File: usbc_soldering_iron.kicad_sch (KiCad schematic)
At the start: 87 parts, among them J1 DBG, J2 TIP_L, J3 USB_C_Receptacle_USB2.0_14P, J4 TIP_H, J5 TIP_K, J6 OLED, J7 LED RING, Q1 DMP6023LE, Q2 MMBT3904, SW1 RST, SW2 B1, SW3 B2, SW4 B3, SW5 BS, U1 SRV05-4, U2 MCP6001-OT, U3 CH32V203GxUx, U4 AP63201WU, U5 FUSB302BMPX, U6 TLV333IDBVR, U7 SC7A20

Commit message: board dimensions and different components
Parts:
- removed C1, C12, C15: 100n, Capacitor_SMD:C_0805_2012Metric, symbol Device:C_Small
- removed C5: 22u, Capacitor_SMD:C_0805_2012Metric, symbol Device:C_Small
- removed Q1: DMP6023LE, Package_TO_SOT_SMD:SOT-223-3_TabPin2, symbol Transistor_FET:Q_PMOS_GDS
- removed SW1: RST, Button_Switch_SMD:SW_SPST_TS-1088-xR020, symbol Switch:SW_Push
- removed SW4: B3, Button_Switch_SMD:SW_SPST_TS-1088-xR020, symbol Switch:SW_Push
- removed U1: SRV05-4, Package_TO_SOT_SMD:SOT-23-6, symbol Power_Protection:SRV05-4
- added H1, H2: MountingHole, MountingHole:MountingHole_2.2mm_M2, symbol Mechanical:MountingHole
- added Q3: DMP3013SFV, Package_SON:Diodes_PowerDI3333-8, symbol Transistor_FET:DMP3013SFV
- added TP1, TP7: TP_PD1, TestPoint:TestPoint_Pad_D1.0mm, symbol Connector:TestPoint
- added U8: TPD4E05U06DQA, Package_SON:USON-10_2.5x1.0mm_P0.5mm, symbol Power_Protection:TPD4E05U06DQA
- C1: renamed from C8; footprint Capacitor_SMD:C_0805_2012Metric -> Capacitor_SMD:C_0603_1608Metric
- C10: renamed from C3; footprint Capacitor_SMD:C_0805_2012Metric -> Capacitor_SMD:C_0603_1608Metric
- C11: renamed from C14; footprint Capacitor_SMD:C_0805_2012Metric -> Capacitor_SMD:C_0603_1608Metric
- C12: renamed from C6; footprint Capacitor_SMD:C_0805_2012Metric -> Capacitor_SMD:C_0603_1608Metric
- C13: renamed from C32; footprint Capacitor_SMD:C_0805_2012Metric -> Capacitor_SMD:C_0603_1608Metric
- C15: renamed from C34; footprint Capacitor_SMD:C_0805_2012Metric -> Capacitor_SMD:C_0603_1608Metric
- C16: renamed from C33; footprint Capacitor_SMD:C_0805_2012Metric -> Capacitor_SMD:C_0603_1608Metric
- C17: renamed from C29; footprint Capacitor_SMD:C_0805_2012Metric -> Capacitor_SMD:C_0603_1608Metric
- C18: renamed from C26; footprint Capacitor_SMD:C_0805_2012Metric -> Capacitor_SMD:C_0603_1608Metric
- C19: renamed from C27; footprint Capacitor_SMD:C_0805_2012Metric -> Capacitor_SMD:C_0603_1608Metric
- C2: renamed from C9; footprint Capacitor_SMD:C_0805_2012Metric -> Capacitor_SMD:C_0603_1608Metric
- C20: renamed from C28; footprint Capacitor_SMD:C_0805_2012Metric -> Capacitor_SMD:C_0603_1608Metric
- C21: renamed from C30; footprint Capacitor_SMD:C_0805_2012Metric -> Capacitor_SMD:C_0603_1608Metric
- C22: renamed from C31; footprint Capacitor_SMD:C_0805_2012Metric -> Capacitor_SMD:C_0603_1608Metric
- C23: footprint Capacitor_SMD:C_0805_2012Metric -> Capacitor_SMD:C_0603_1608Metric
- C28: renamed from C24; footprint Capacitor_SMD:C_0805_2012Metric -> Capacitor_SMD:C_0603_1608Metric
- C3: renamed from C7; footprint Capacitor_SMD:C_0805_2012Metric -> Capacitor_SMD:C_0603_1608Metric
- C30: renamed from C16; footprint Capacitor_SMD:C_0805_2012Metric -> Capacitor_SMD:C_0603_1608Metric
- C31: renamed from C25; footprint Capacitor_SMD:C_0805_2012Metric -> Capacitor_SMD:C_0603_1608Metric
- C32: renamed from C21; footprint Capacitor_SMD:C_0805_2012Metric -> Capacitor_SMD:C_0603_1608Metric
- C5: renamed from C11; footprint Capacitor_SMD:C_0805_2012Metric -> Capacitor_SMD:C_0603_1608Metric
- C6: renamed from C10; footprint Capacitor_SMD:C_0805_2012Metric -> Capacitor_SMD:C_0603_1608Metric
- C7: renamed from C2; footprint Capacitor_SMD:C_0805_2012Metric -> Capacitor_SMD:C_0603_1608Metric
- C9: renamed from C13; footprint Capacitor_SMD:C_0805_2012Metric -> Capacitor_SMD:C_0603_1608Metric
- J1: renamed from J3; footprint Connector_USB:USB_C_Receptacle_G-Switch_GT-USB-7010ASV -> Connector_USB:USB_C_Receptacle_G-Switch_GT-USB-7025
- L1: footprint Inductor_SMD:L_0805_2012Metric -> Inductor_SMD:L_Changjiang_FTC201607S
- R1: footprint Resistor_SMD:R_0805_2012Metric -> Resistor_SMD:R_0603_1608Metric
- R10: renamed from R22; footprint Resistor_SMD:R_0805_2012Metric -> Resistor_SMD:R_0603_1608Metric
- R11: renamed from R3; footprint Resistor_SMD:R_0805_2012Metric -> Resistor_SMD:R_0603_1608Metric
- R12: renamed from R4; footprint Resistor_SMD:R_0805_2012Metric -> Resistor_SMD:R_0603_1608Metric
- R13: renamed from R23; footprint Resistor_SMD:R_0805_2012Metric -> Resistor_SMD:R_0603_1608Metric
- R14: renamed from R21; footprint Resistor_SMD:R_0805_2012Metric -> Resistor_SMD:R_0603_1608Metric
- R15: renamed from R13; footprint Resistor_SMD:R_0805_2012Metric -> Resistor_SMD:R_0603_1608Metric
- R16: renamed from R14; footprint Resistor_SMD:R_0805_2012Metric -> Resistor_SMD:R_0603_1608Metric
- R17: renamed from R15; footprint Resistor_SMD:R_0805_2012Metric -> Resistor_SMD:R_0603_1608Metric
- R18: renamed from R16; footprint Resistor_SMD:R_0805_2012Metric -> Resistor_SMD:R_0603_1608Metric
- R19: renamed from R12; footprint Resistor_SMD:R_0805_2012Metric -> Resistor_SMD:R_0603_1608Metric
- R2: renamed from R5; footprint Resistor_SMD:R_0805_2012Metric -> Resistor_SMD:R_0603_1608Metric
- R20: renamed from R11; footprint Resistor_SMD:R_0805_2012Metric -> Resistor_SMD:R_0603_1608Metric
- R21: renamed from R10; footprint Resistor_SMD:R_0805_2012Metric -> Resistor_SMD:R_0603_1608Metric
- R22: renamed from R19; footprint Resistor_SMD:R_0805_2012Metric -> Resistor_SMD:R_0603_1608Metric
- R23: renamed from R20; footprint Resistor_SMD:R_0805_2012Metric -> Resistor_SMD:R_0603_1608Metric
- R25: renamed from R17; footprint Resistor_SMD:R_0805_2012Metric -> Resistor_SMD:R_0603_1608Metric
- R3: renamed from R6; footprint Resistor_SMD:R_0805_2012Metric -> Resistor_SMD:R_0603_1608Metric
- R4: renamed from R8; footprint Resistor_SMD:R_0805_2012Metric -> Resistor_SMD:R_0603_1608Metric
- R5: renamed from R7; footprint Resistor_SMD:R_0805_2012Metric -> Resistor_SMD:R_0603_1608Metric
- R6: renamed from R2; footprint Resistor_SMD:R_0805_2012Metric -> Resistor_SMD:R_0603_1608Metric
- R7: renamed from R24; footprint Resistor_SMD:R_0805_2012Metric -> Resistor_SMD:R_0603_1608Metric
- R8: renamed from R25; footprint Resistor_SMD:R_0805_2012Metric -> Resistor_SMD:R_0603_1608Metric
- R9: renamed from R18; footprint Resistor_SMD:R_0805_2012Metric -> Resistor_SMD:R_0603_1608Metric
- renumbered C4 to C14, C22 to C24, C20 to C25, C19 to C26, C18 to C27, C17 to C29, J1 to J2, J7 to J3, J6 to J4, J4 to J5, J5 to J6, J2 to J7, Q2 to Q1, R9 to R24, SW5 to SW4, TP1 to TP2, TP2 to TP3, TP3 to TP4, TP4 to TP5, TP5 to TP6, U3 to U1, U5 to U2, U7 to U5, U2 to U6, U6 to U7
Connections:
- net CC1: now also U8.5 (D2-)
- net CC2: now also U8.1 (D1+)
- net GND: now also U8.3 (GND), U8.8 (GND)
- net NRST: now also TP7.1
- net SHUNT_L: now also Q3.5 (D)
- net TIP_H: now also Q3.1 (S), Q3.2 (S), Q3.3 (S)
- net JDP: now reaches J1.A6 (D+), J1.B6 (D+), R3.1
- net JDP: now also U8.2 (D1-)
- net JDN: now reaches J1.A7 (D-), J1.B7 (D-), R2.1
- net JDN: now also U8.4 (D2+)
- net at R20.2, R21.1: now also Q3.4 (G)
- net BTN3 renamed PB3
- net PB3: now also TP1.1
- no-connect marks 2 -> 6
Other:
- note removed: "REVIEW"
- moved on the sheet: C11, C13, C3, R13, R2, R3, SW3, SW4

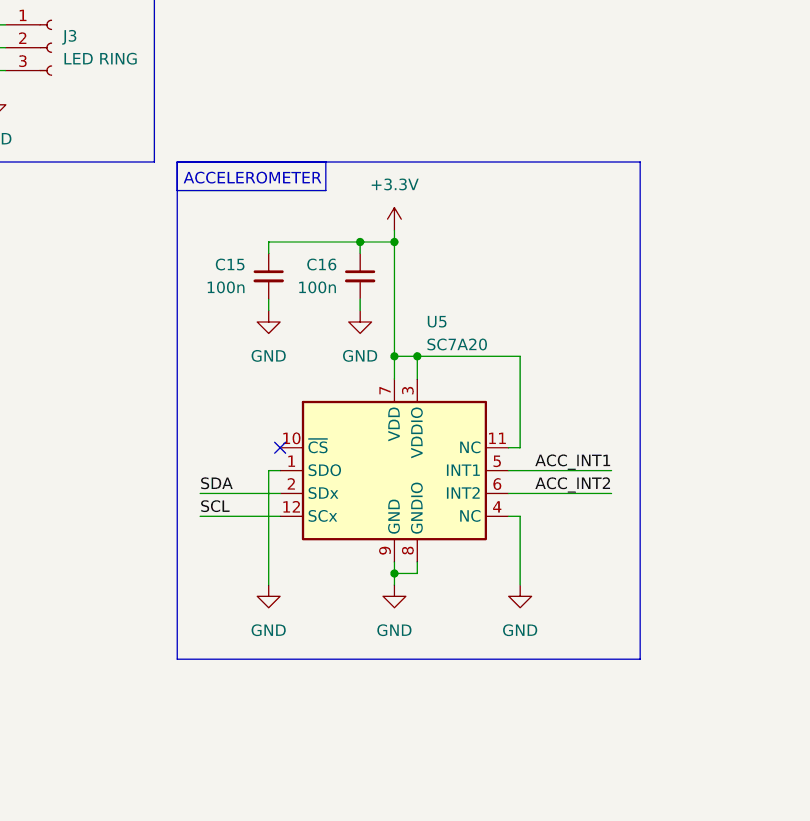
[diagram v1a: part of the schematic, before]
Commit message: some things needed to be 0805
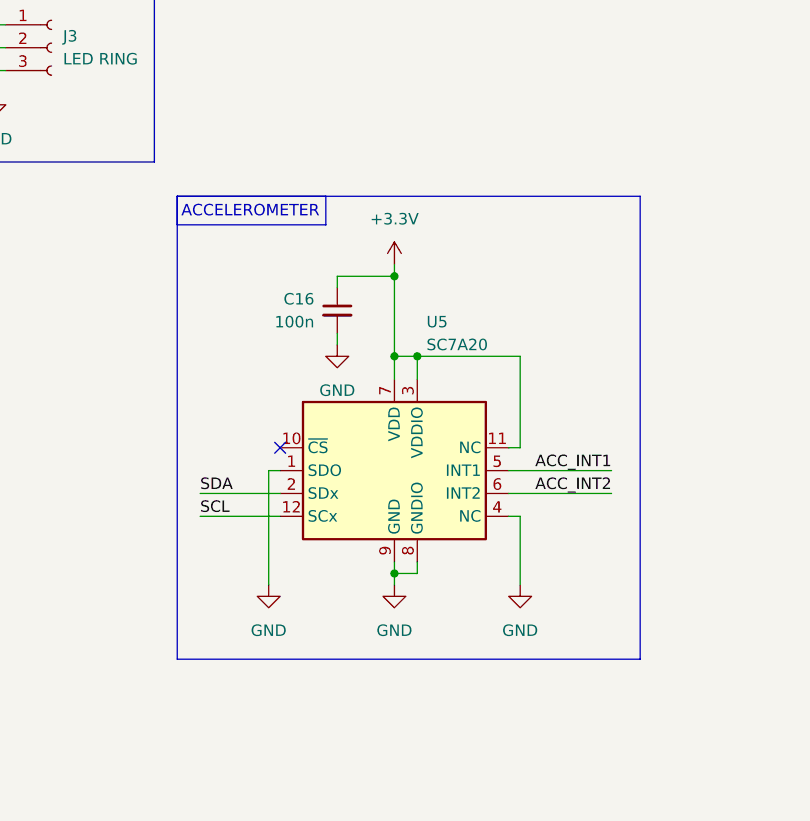
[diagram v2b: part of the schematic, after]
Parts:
- removed C15: 100n, Capacitor_SMD:C_0603_1608Metric, symbol Device:C_Small
- C30, C7: footprint Capacitor_SMD:C_0603_1608Metric -> Capacitor_SMD:C_0805_2012Metric
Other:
- moved on the sheet: C16
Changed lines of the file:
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@@
 	)
 	(rectangle
-		(start 185.42 140.97)
+		(start 185.42 144.78)
 		(end 236.855 196.215)
 		(stroke
@@
 	)
 	(rectangle
-		(start 185.42 140.97)
-		(end 201.93 144.145)
+		(start 185.42 144.78)
+		(end 201.93 147.955)
 		(stroke
 			(width 0)
@@
 	(text "ACCELEROMETER"
 		(exclude_from_sim no)
-		(at 193.802 143.002 0)
+		(at 193.548 146.558 0)
 		(effects
 			(font
@@
 	)
 	(junction
-		(at 205.74 149.86)
-		(diameter 0)
-		(color 0 0 0 0)
-	)
-	(junction
 		(at 46.99 49.53)
 		(diameter 0)
@@
 	)
 	(junction
-		(at 209.55 149.86)
+		(at 383.54 149.86)
 		(diameter 0)
 		(color 0 0 0 0)
 	)
 	(junction
-		(at 383.54 149.86)
+		(at 356.87 86.36)
 		(diameter 0)
 		(color 0 0 0 0)
 	)
 	(junction
-		(at 356.87 86.36)
+		(at 209.55 153.67)
 		(diameter 0)
 		(color 0 0 0 0)
@@
 		)
 	)
-	(wire
-		(pts
-			(xy 195.58 151.13) (xy 195.58 149.86)
-		)
-		(stroke
-			(width 0)
-			(type default)
-		)
-	)
 	(polyline
 		(pts
@@
 	(wire
 		(pts
-			(xy 209.55 148.59) (xy 209.55 149.86)
+			(xy 209.55 152.4) (xy 209.55 153.67)
 		)
 		(stroke
@@
 	(wire
 		(pts
-			(xy 205.74 151.13) (xy 205.74 149.86)
+			(xy 203.2 154.94) (xy 203.2 153.67)
 		)
 		(stroke
@@
 	(wire
 		(pts
-			(xy 205.74 156.21) (xy 205.74 157.48)
+			(xy 203.2 160.02) (xy 203.2 161.29)
 		)
 		(stroke
@@
 	(wire
 		(pts
-			(xy 209.55 149.86) (xy 209.55 162.56)
-		)
-		(stroke
-			(width 0)
-			(type default)
-		)
-	)
-	(wire
-		(pts
 			(xy 152.4 88.9) (xy 162.56 88.9)
 		)
@@
 	(wire
 		(pts
+			(xy 209.55 153.67) (xy 209.55 162.56)
+		)
+		(stroke
+			(width 0)
+			(type default)
+		)
+	)
+	(wire
+		(pts
 			(xy 369.57 138.43) (xy 375.92 138.43)
 		)
@@
 	(wire
 		(pts
-			(xy 195.58 156.21) (xy 195.58 157.48)
-		)
-		(stroke
-			(width 0)
-			(type default)
-		)
-	)
-	(wire
-		(pts
 			(xy 381 148.59) (xy 381 157.48)
 		)
@@
 	(wire
 		(pts
-			(xy 205.74 149.86) (xy 209.55 149.86)
+			(xy 203.2 153.67) (xy 209.55 153.67)
 		)
 		(stroke
@@
 	(wire
 		(pts
-			(xy 195.58 149.86) (xy 205.74 149.86)
-		)
-		(stroke
-			(width 0)
-			(type default)
-		)
-	)
-	(wire
-		(pts
 			(xy 205.74 68.58) (xy 228.6 68.58)
 		)
@@
 			)
 		)
-		(property "Footprint" "Capacitor_SMD:C_0603_1608Metric"
+		(property "Footprint" "Capacitor_SMD:C_0805_2012Metric"
 			(at 106.68 31.75 0)
 			(effects
@@
 			)
 		)
-		(property "Footprint" "Capacitor_SMD:C_0603_1608Metric"
+		(property "Footprint" "Capacitor_SMD:C_0805_2012Metric"
 			(at 383.54 90.17 0)
 			(effects
@@
 	)
 	(symbol
-		(lib_id "Device:C_Small")
-		(at 195.58 153.67 0)
-		(mirror y)
-		(unit 1)
-		(exclude_from_sim no)
-		(in_bom yes)
-		(on_board yes)
-		(dnp no)
-		(property "Reference" "C15"
-			(at 193.04 152.4062 0)
-			(effects
-				(font
-					(size 1.27 1.27)
-				)
-				(justify left)
-			)
-		)
-		(property "Value" "100n"
-			(at 193.04 154.9462 0)
-			(effects
-				(font
-					(size 1.27 1.27)
-				)
-				(justify left)
-			)
-		)
-		(property "Footprint" "Capacitor_SMD:C_0603_1608Metric"
-			(at 195.58 153.67 0)
-			(effects
-				(font
-					(size 1.27 1.27)
-				)
-				(hide yes)
-			)
-		)
-		(property "Datasheet" "~"
-			(at 195.58 153.67 0)
-			(effects
-				(font
-					(size 1.27 1.27)
-				)
-				(hide yes)
-			)
-		)
-		(property "Description" "Unpolarized capacitor, small symbol"
-			(at 195.58 153.67 0)
-			(effects
-				(font
-					(size 1.27 1.27)
-				)
-				(hide yes)
-			)
-		)
-		(pin "2"
-		)
-		(pin "1"
-		)
-		(instances
-			(project "usbc_soldering_iron"
-				(path "/7095b018-eac3-4b01-b374-28e3216c4fd8"
-					(reference "C15")
-					(unit 1)
-				)
-			)
-		)
-	)
-	(symbol
 		(lib_id "Switch:SW_Push")
 		(at 118.11 181.61 90)
@@
 	(symbol
 		(lib_id "Device:C_Small")
-		(at 205.74 153.67 0)
+		(at 203.2 157.48 0)
 		(mirror y)
 		(unit 1)
@@
 		(dnp no)
 		(property "Reference" "C16"
-			(at 203.2 152.4062 0)
+			(at 200.66 156.2162 0)
 			(effects
 				(font
@@
 		)
 		(property "Value" "100n"
-			(at 203.2 154.9462 0)
+			(at 200.66 158.7562 0)
 			(effects
 				(font
@@
 		)
 		(property "Footprint" "Capacitor_SMD:C_0603_1608Metric"
-			(at 205.74 153.67 0)
+			(at 203.2 157.48 0)
 			(effects
 				(font
@@
 		)
 		(property "Datasheet" "~"
-			(at 205.74 153.67 0)
+			(at 203.2 157.48 0)
 			(effects
 				(font
@@
 		)
 		(property "Description" "Unpolarized capacitor, small symbol"
-			(at 205.74 153.67 0)
+			(at 203.2 157.48 0)
 			(effects
 				(font
@@
 	(symbol
 		(lib_id "power:+3.3V")
-		(at 209.55 148.59 0)
+		(at 209.55 152.4 0)
 		(unit 1)
 		(exclude_from_sim no)
@@
 		(fields_autoplaced yes)
 		(property "Reference" "#PWR044"
-			(at 209.55 152.4 0)
+			(at 209.55 156.21 0)
 			(effects
 				(font
@@
 		)
 		(property "Value" "+3.3V"
-			(at 209.55 143.51 0)
+			(at 209.55 147.32 0)
 			(effects
 				(font
@@
 		)
 		(property "Footprint" ""
-			(at 209.55 148.59 0)
+			(at 209.55 152.4 0)
 			(effects
 				(font
@@
 		)
 		(property "Datasheet" ""
-			(at 209.55 148.59 0)
+			(at 209.55 152.4 0)
 			(effects
 				(font
@@
 		)
 		(property "Description" "Power symbol creates a global label with name \"+3.3V\""
-			(at 209.55 148.59 0)
+			(at 209.55 152.4 0)
 			(effects
 				(font
@@
 	(symbol
 		(lib_id "power:GND")
-		(at 205.74 157.48 0)
+		(at 203.2 161.29 0)
 		(unit 1)
 		(exclude_from_sim no)
@@
 		(fields_autoplaced yes)
 		(property "Reference" "#PWR043"
-			(at 205.74 163.83 0)
+			(at 203.2 167.64 0)
 			(effects
 				(font
@@
 		)
 		(property "Value" "GND"
-			(at 205.74 162.56 0)
+			(at 203.2 166.37 0)
 			(effects
 				(font
@@
 		)
 		(property "Footprint" ""
-			(at 205.74 157.48 0)
+			(at 203.2 161.29 0)
 			(effects
 				(font
@@
 		)
 		(property "Datasheet" ""
-			(at 205.74 157.48 0)
+			(at 203.2 161.29 0)
 			(effects
 				(font
@@
 		)
 		(property "Description" "Power symbol creates a global label with name \"GND\" , ground"
-			(at 205.74 157.48 0)
+			(at 203.2 161.29 0)
 			(effects
 				(font
@@
 					(unit 1)
 				)
-			)
-		)
-	)
-	(symbol
-		(lib_id "power:GND")
-		(at 195.58 157.48 0)
-		(unit 1)
-		(exclude_from_sim no)
-		(in_bom yes)
-		(on_board yes)
-		(dnp no)
-		(fields_autoplaced yes)
-		(property "Reference" "#PWR040"
-			(at 195.58 163.83 0)
-			(effects
-				(font
-					(size 1.27 1.27)
-				)
-				(hide yes)
-			)
-		)
-		(property "Value" "GND"
-			(at 195.58 162.56 0)
-			(effects
-				(font
-					(size 1.27 1.27)
-				)
-			)
-		)
-		(property "Footprint" ""
-			(at 195.58 157.48 0)
-			(effects
-				(font
-					(size 1.27 1.27)
-				)
-				(hide yes)
-			)
-		)
-		(property "Datasheet" ""
-			(at 195.58 157.48 0)
-			(effects
-				(font
-					(size 1.27 1.27)
-				)
-				(hide yes)
-			)
-		)
-		(property "Description" "Power symbol creates a global label with name \"GND\" , ground"
-			(at 195.58 157.48 0)
-			(effects
-				(font
-					(size 1.27 1.27)
-				)
-				(hide yes)
-			)
-		)
-		(pin "1"
-		)
-		(instances
-			(project "usbc_soldering_iron"
-				(path "/7095b018-eac3-4b01-b374-28e3216c4fd8"
-					(reference "#PWR040")
-					(unit 1)
-				)
